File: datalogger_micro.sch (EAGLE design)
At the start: 41 parts, among them IC1 DS3231/SO, IC3 LD117AS33TR, M0 PAT, M1 PAT

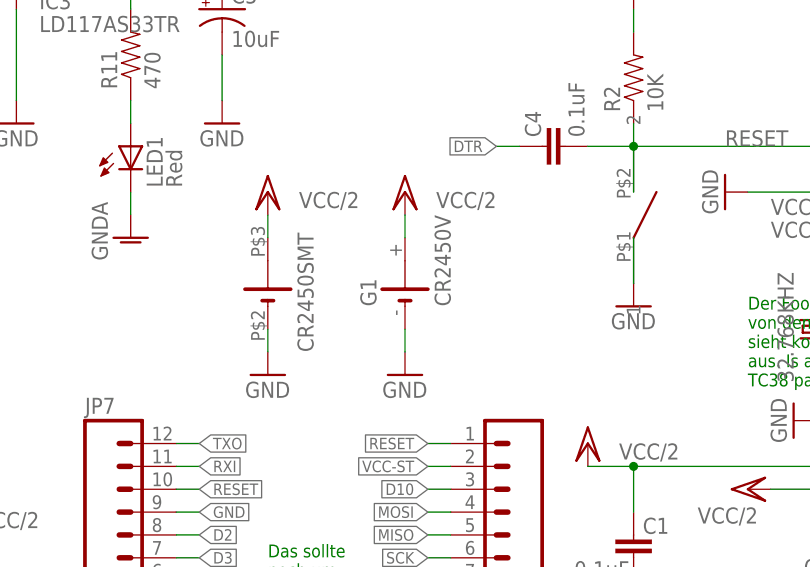
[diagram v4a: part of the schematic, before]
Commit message: one-sided
moved layout to one sided again, use SMT battery pack.
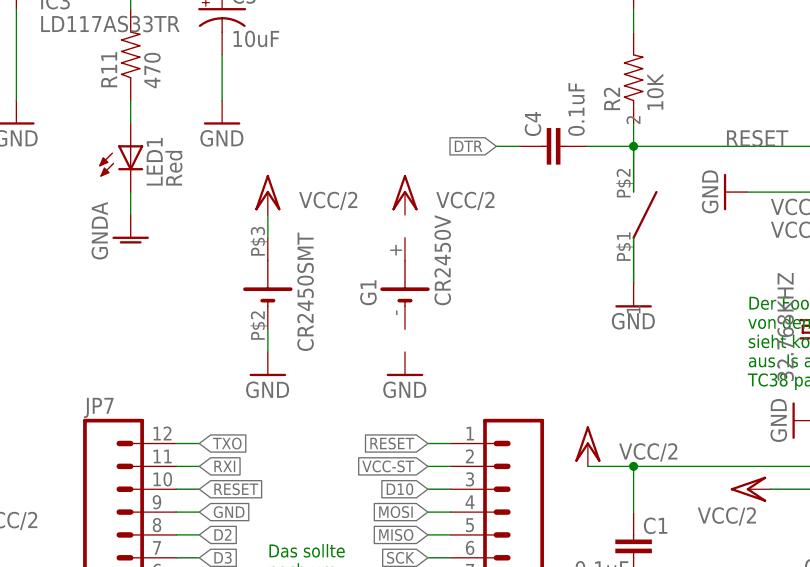
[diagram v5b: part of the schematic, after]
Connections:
- net GND: no longer G1.-
- net VCC/2: no longer G1.+
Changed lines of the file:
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@@
 <?xml version="1.0" encoding="utf-8"?>
 <!DOCTYPE eagle SYSTEM "eagle.dtd">
-<eagle version="7.2.0">
+<eagle version="7.3.0">
 <drawing>
 <settings>
@@
 <pinref part="U$3" gate="G$1" pin="-"/>
 </segment>
-<segment>
-<pinref part="GND19" gate="1" pin="GND"/>
-<pinref part="G1" gate="1" pin="-"/>
-<wire x1="96.52" y1="132.08" x2="96.52" y2="134.62" width="0.1524" layer="91"/>
-</segment>
 </net>
 <net name="RESET" class="0">
@@
 <pinref part="U$3" gate="G$1" pin="+"/>
 </segment>
-<segment>
-<pinref part="G1" gate="1" pin="+"/>
-<pinref part="VCC-BAT8" gate="G$1" pin="VCC/2"/>
-<wire x1="96.52" y1="144.78" x2="96.52" y2="147.32" width="0.1524" layer="91"/>
-</segment>
-</net>
+</net>

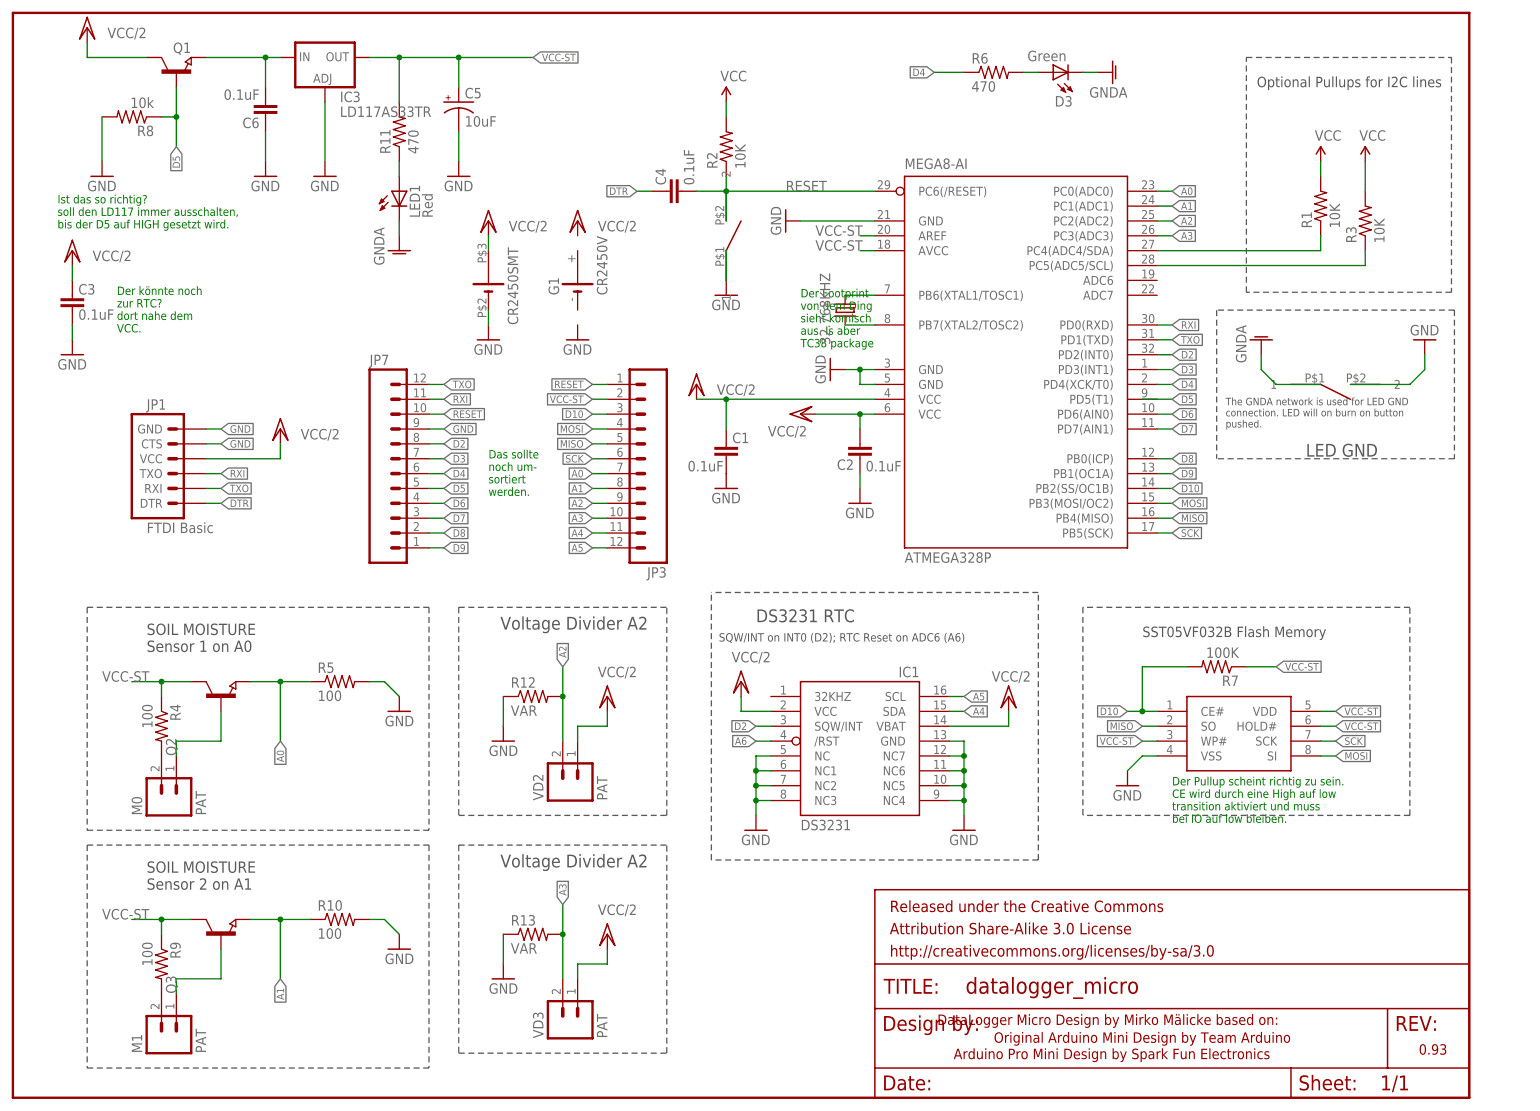
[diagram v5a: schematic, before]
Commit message: schematic adaptions
a lot of schematic adaptions. included various C and Rs were neceassary.
MOSFET instead of Transistor on LM1117..
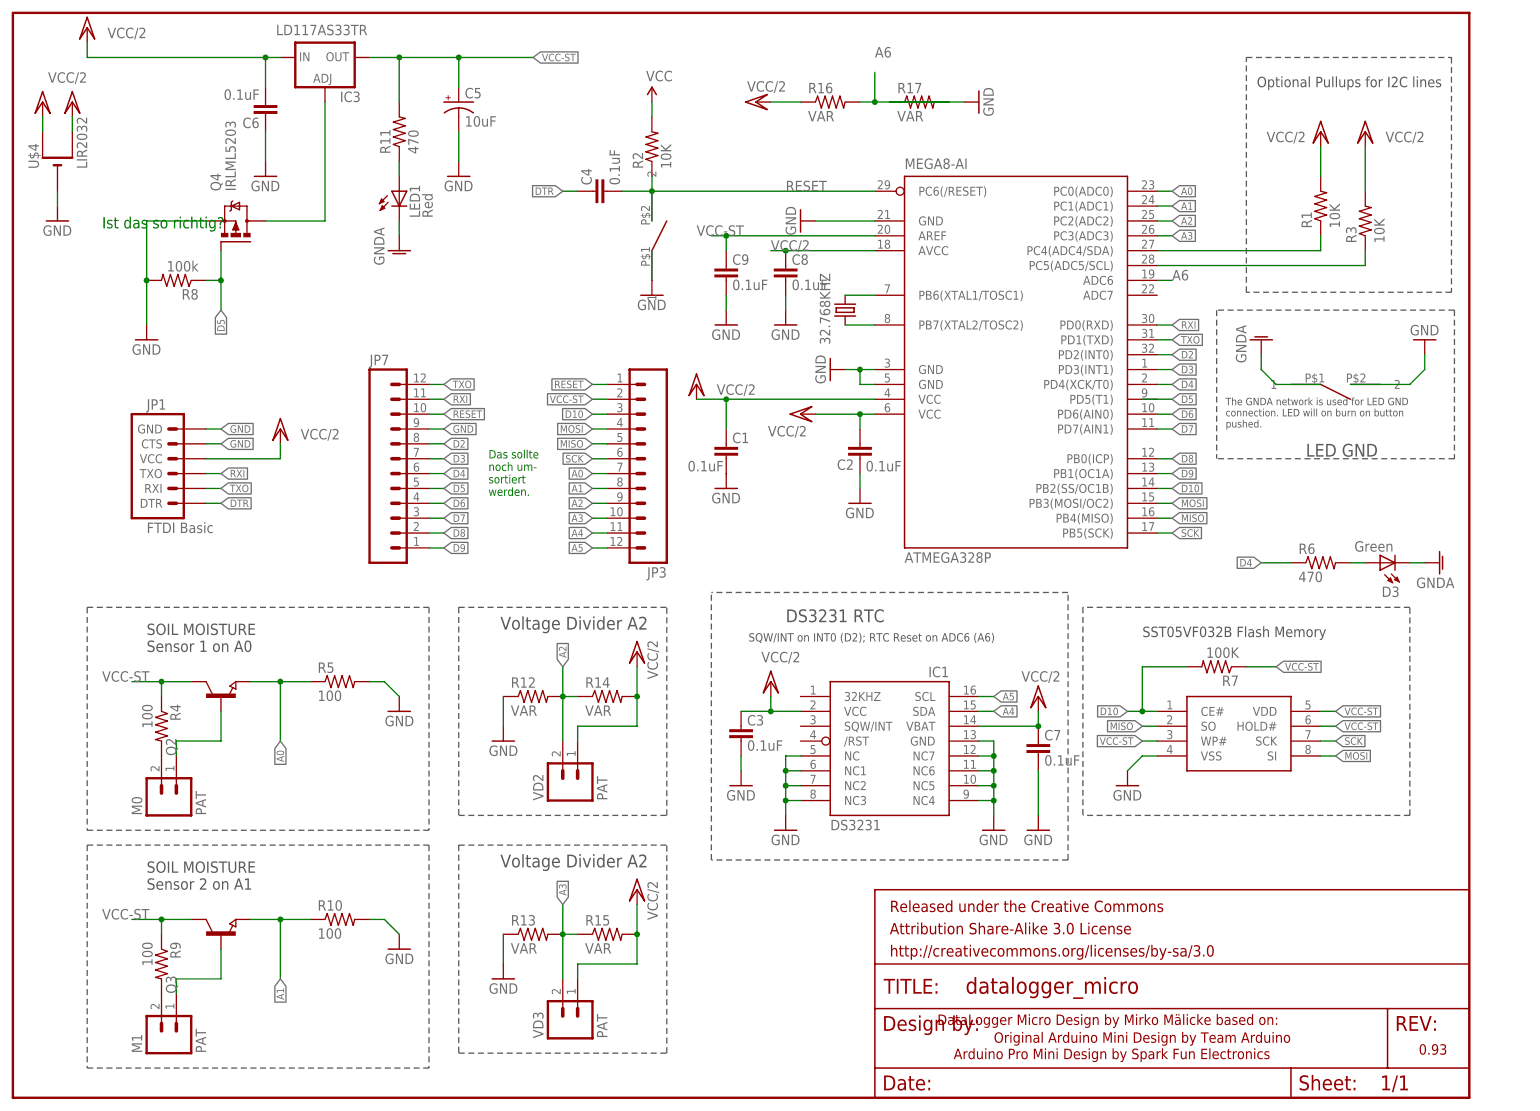
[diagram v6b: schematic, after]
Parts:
- removed G1: CR2450V, battery:CR2450V
- removed Q1: (no value), semicon-smd-ipc:NPN-TRANSISTOR_SOT23
- removed U$3: CR2450SMT, battery:CR2450SMT
- added C7, C8, C9: 0.1uF, SparkFun:CAP0603-CAP
- added Q4: IRLML5203, transistor-power:IRLML5203
- added R14, R15, R16, R17: VAR, SparkFun:RESISTOR0603-RES
- added U$4: LIR2032, adafruit:CR2032SMT
- R8: value 10k -> 100k
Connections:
- net A2: now also R14.1
- net A3: now also R15.1
- net A6: now also ATMEGA328P.ADC6, R16.2, R17.2; no longer IC1./RST
- net D2: no longer IC1.SQW/INT
- net D5: now also Q4.G; no longer Q1.B
- net GND: now also C7.1, C8.1, C9.1, Q4.S, R17.1, U$4.-; no longer IC3.ADJ, U$3.-
- net N$1: now also IC3.ADJ, Q4.D; no longer C6.1, IC3.IN, Q1.E
- net VCC-ST: now also C9.2; no longer ATMEGA328P.AVCC, R1.2, R3.2
- net VCC/2: now also ATMEGA328P.AVCC, C6.1, C7.2, C8.2, IC3.IN, R1.2, R14.2, R15.2, R16.1, R3.2, U$4.+, U$4.+1; no longer Q1.C, U$3.+
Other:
- note added: "Ist das so richtig?"
- note removed: "Der Footprint von dem Ding sieht komisch aus. Is aber TC38 package"
- note removed: "Der Pullup scheint richtig zu sein. CE wird durch eine High auf low transition aktiviert und muss bei IO auf low bleiben."
- note removed: "Der könnte noch zur RTC? dort nahe dem VCC."
- note removed: "Ist das so richtig? soll den LD117 immer ausschalten, bis der D5 auf HIGH gesetzt wird."
- moved on the sheet: C3, C4, D3, IC1, R2, R6, R8

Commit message: schematics finalized
schematics are finalized and will be verified
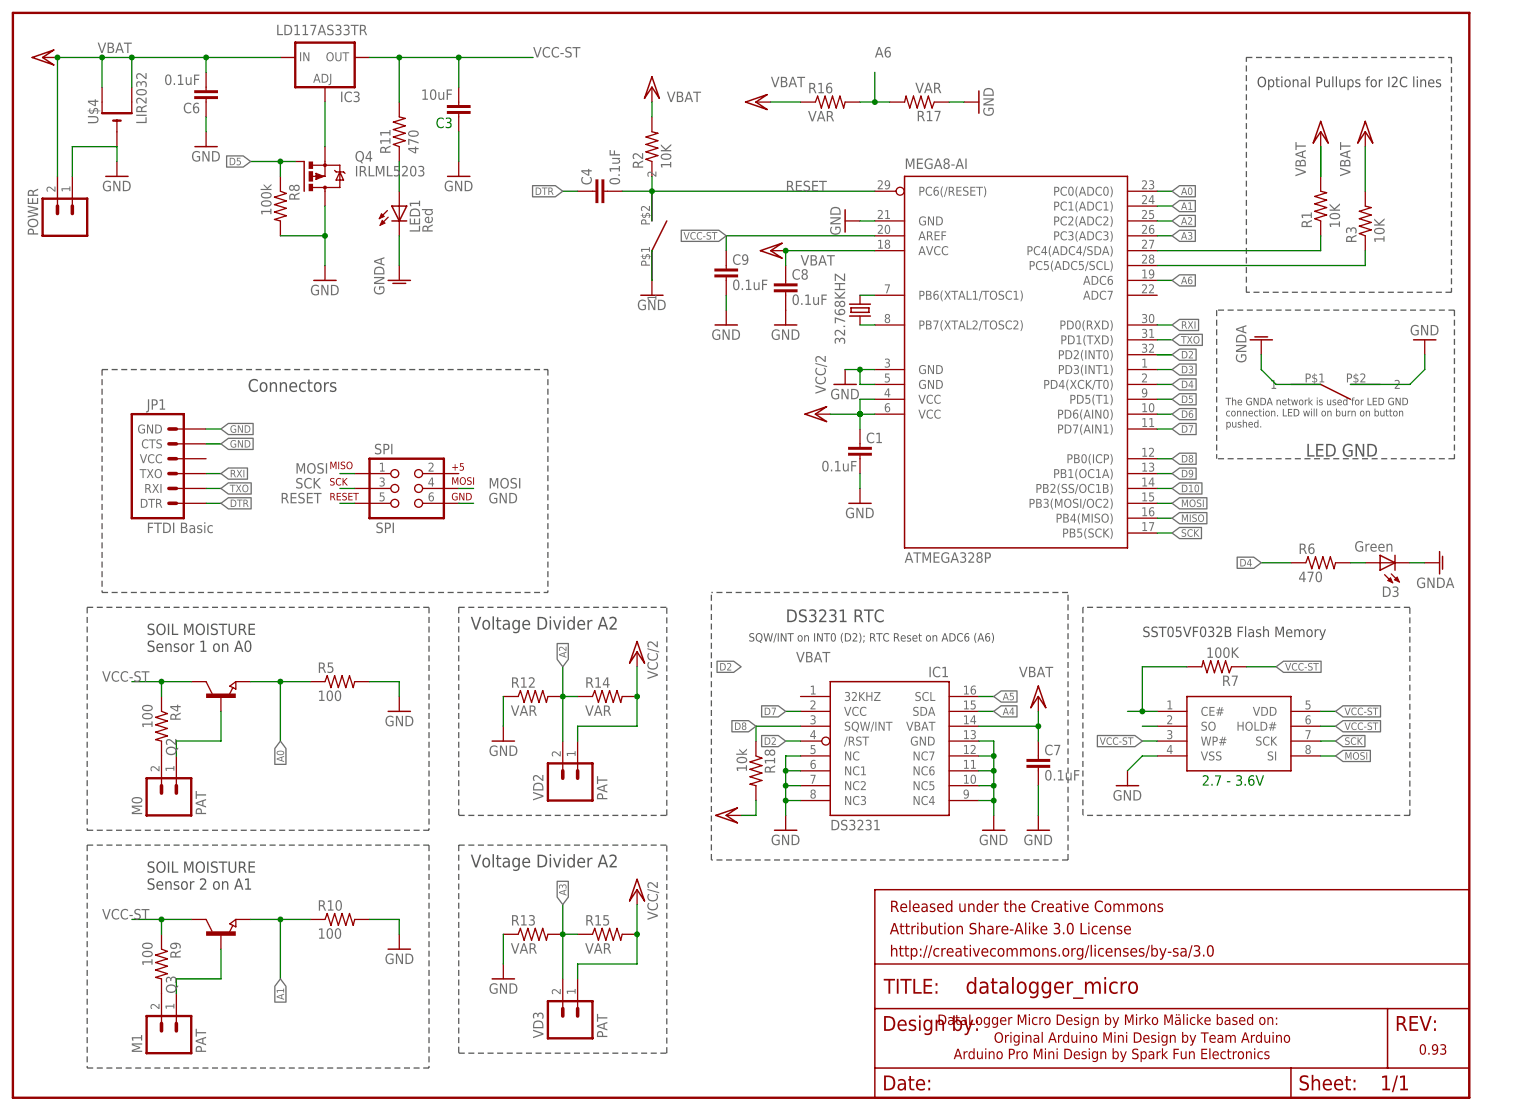
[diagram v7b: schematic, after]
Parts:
- removed C2: 0.1uF, SparkFun:CAP0603-CAP
- removed C5: 10uF, rcl:CPOL-USE2.5-5
- removed JP3, JP7: M12PTH, SparkFun:M12PTH
- added POWER: (no value), SparkFun:M02PTH
- added R18: 10k, SparkFun:RESISTOR0603-RES
- added SPI: SPI, SparkFun-Connectors:AVR_SPI_PRG_62X3_LOCK
- C3: value 0.1uF -> 10uF; device SparkFun:CAP0603-CAP -> SparkFun:CAP1206
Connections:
- removed net VCC/2: ATMEGA328P.AVCC, ATMEGA328P.VCC@1, ATMEGA328P.VCC@2, C1.2, C2.1, C3.2, C6.1, C7.2, C8.2, IC1.VBAT, IC1.VCC, IC3.IN, JP1.VCC, R1.2, R14.2, R15.2, R16.1, R3.2, U$4.+, U$4.+1, VD2.1, VD3.1
- new net VBAT: ATMEGA328P.AVCC, ATMEGA328P.VCC@1, ATMEGA328P.VCC@2, C1.2, C6.1, C7.2, C8.2, IC1.VBAT, IC3.IN, POWER.2, R1.2, R14.2, R15.2, R16.1, R18.2, R2.2, R3.2, U$4.+, U$4.+1, VD2.1, VD3.1
- net A0: no longer JP3.7
- net A1: no longer JP3.8
- net A2: no longer JP3.9
- net A3: no longer JP3.10
- net A4: no longer JP3.11
- net A5: no longer JP3.12
- net D10: no longer JP3.3
- net D2: now also IC1./RST; no longer JP7.8
- net D3: no longer JP7.7
- net D4: no longer JP7.6
- net D5: no longer JP7.5
- net D6: no longer JP7.4
- net D7: now also IC1.VCC; no longer JP7.3
- net D8: now also IC1.SQW/INT, R18.1; no longer JP7.2
- net D9: no longer JP7.1
- net GND: now also C3.2, POWER.1, Q4.D, SPI.6; no longer C2.2, C3.1, C5.-, JP7.9, Q4.S
- net MISO: no longer JP3.5
- net MOSI: now also SPI.1, SPI.4; no longer JP3.4
- net N$1: now also Q4.S; no longer Q4.D
- net RESET: now also SPI.5; no longer JP3.1, JP7.10
- net RXI: no longer JP7.11
- net SCK: now also SPI.3; no longer JP3.6
- net TXO: no longer JP7.12
- net VCC-ST: now also C3.1; no longer C5.+, JP3.2, R2.2
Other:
- note added: "2.7 - 3.6V"
- note added: "Connectors"
- note removed: "Das sollte noch um- sortiert werden."
- note removed: "Ist das so richtig?"
- moved on the sheet: 32.768KHZ, C1, C3, C6, C7, C8, LED1, Q4, R17, R8, U$4

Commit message: bug fix
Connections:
- net MISO: now also SPI.1
- net MOSI: no longer SPI.1
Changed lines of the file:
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@@
 <?xml version="1.0" encoding="utf-8"?>
 <!DOCTYPE eagle SYSTEM "eagle.dtd">
-<eagle version="7.3.0">
+<eagle version="7.2.0">
 <drawing>
 <settings>
@@
 <pinref part="U$2" gate="SST25VF032B" pin="SO"/>
 </segment>
+<segment>
+<pinref part="SPI" gate="G$1" pin="1"/>
+<wire x1="58.42" y1="106.68" x2="55.88" y2="106.68" width="0.1524" layer="91"/>
+<label x="48.26" y="106.68" size="1.778" layer="95"/>
+</segment>
 </net>
 <net name="MOSI" class="0">
@@
 </segment>
 <segment>
-<wire x1="55.88" y1="106.68" x2="58.42" y2="106.68" width="0.1524" layer="91"/>
-<label x="48.26" y="106.68" size="1.778" layer="95"/>
-<pinref part="SPI" gate="G$1" pin="1"/>
-</segment>
-<segment>
